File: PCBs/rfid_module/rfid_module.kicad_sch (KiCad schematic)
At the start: 0 parts

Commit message: RFID Module progress
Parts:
- added U101: Watch_Module_Outline_V1, watch_footprints:Watch Module Outline V1, symbol watch_symbols_lib:Watch_Module_Outline_V1
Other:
- added sheet Boost Converter (boost_converter.kicad_sch)
- added sheet Pogo Connector (pogo_connector.kicad_sch)
- added sheet STM32G0 (stm32g0.kicad_sch)
- sheet RFID ports: added CARRIER, OUT, OUTN, PULL, RF_IN, SHDN, VRF; removed none
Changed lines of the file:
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@@
 (kicad_sch (version 20230121) (generator eeschema)
   (paper "A4")
-  (sheet (at 121.92 66.04) (size 43.18 43.18) (fields_autoplaced)
-    (stroke (width 0.1524) (type solid))
-    (fill (color 0 0 0 0.0000))
-    (property "Sheetname" "RFID" (at 121.92 65.3284 0)
+  (wire (pts (xy 165.1 99.06) (xy 190.5 99.06))
+    (stroke (width 0) (type default))
+  )
+  (wire (pts (xy 165.1 101.6) (xy 190.5 101.6))
+    (stroke (width 0) (type default))
+  )
+  (wire (pts (xy 215.9 93.98) (xy 228.6 93.98))
+    (stroke (width 0) (type default))
+  )
+  (wire (pts (xy 104.14 78.74) (xy 129.54 78.74))
+    (stroke (width 0) (type default))
+  )
+  (wire (pts (xy 165.1 78.74) (xy 190.5 78.74))
+    (stroke (width 0) (type default))
+  )
+  (wire (pts (xy 228.6 78.74) (xy 228.6 93.98))
+    (stroke (width 0) (type default))
+  )
+  (wire (pts (xy 104.14 81.28) (xy 129.54 81.28))
+    (stroke (width 0) (type default))
+  )
+  (wire (pts (xy 165.1 104.14) (xy 190.5 104.14))
+    (stroke (width 0) (type default))
+  )
+  (wire (pts (xy 165.1 81.28) (xy 190.5 81.28))
+    (stroke (width 0) (type default))
+  )
+  (wire (pts (xy 215.9 78.74) (xy 228.6 78.74))
+    (stroke (width 0) (type default))
+  )
+  (wire (pts (xy 165.1 106.68) (xy 190.5 106.68))
+    (stroke (width 0) (type default))
+  )
+  (wire (pts (xy 165.1 96.52) (xy 190.5 96.52))
+    (stroke (width 0) (type default))
+  )
+  (wire (pts (xy 165.1 93.98) (xy 190.5 93.98))
+    (stroke (width 0) (type default))
+  )
+  (symbol (lib_id "watch_symbols_lib:Watch_Module_Outline_V1") (at 144.78 132.08 0) (unit 1)
+    (in_bom no) (on_board yes) (dnp no) (fields_autoplaced)
+    (property "Reference" "U101" (at 151.13 131.445 0)
+      (effects (font (size 1.27 1.27)) (justify left))
+    )
+    (property "Value" "Watch_Module_Outline_V1" (at 151.13 133.985 0)
+      (effects (font (size 1.27 1.27)) (justify left))
+    )
+    (property "Footprint" "watch_footprints:Watch Module Outline V1" (at 144.78 137.16 0)
+      (effects (font (size 1.27 1.27)) hide)
+    )
+    (property "Datasheet" "" (at 144.78 132.08 0)
+      (effects (font (size 1.27 1.27)) hide)
+    )
+    (instances
+      (project "rfid_module"
+        (path "/7f374643-2d66-4cfc-a525-255f058de0be"
+          (reference "U101") (unit 1)
+        )
+      )
+    )
+  )
+  (sheet (at 190.5 76.2) (size 25.4 7.62) (fields_autoplaced)
+    (stroke (width 0.1524) (type solid) (color 150 115 166 1))
+    (fill (color 225 213 231 1.0000))
+    (property "Sheetname" "Boost Converter" (at 190.5 75.4884 0)
       (effects (font (size 1.27 1.27)) (justify left bottom))
     )
-    (property "Sheetfile" "rfid.kicad_sch" (at 121.92 109.8046 0)
+    (property "Sheetfile" "boost_converter.kicad_sch" (at 190.5 84.4046 0)
       (effects (font (size 1.27 1.27)) (justify left top))
+    )
+    (pin "FB_OFFSET" input (at 190.5 78.74 180)
+      (effects (font (size 1.27 1.27)) (justify left))
+    )
+    (pin "VRF" output (at 215.9 78.74 0)
+      (effects (font (size 1.27 1.27)) (justify right))
+    )
+    (pin "EN" input (at 190.5 81.28 180)
+      (effects (font (size 1.27 1.27)) (justify left))
+    )
+    (instances
+      (project "rfid_module"
+        (path "/7f374643-2d66-4cfc-a525-255f058de0be" (page "5"))
+      )
+    )
+  )
+  (sheet (at 78.74 76.2) (size 25.4 30.48) (fields_autoplaced)
+    (stroke (width 0.1524) (type solid) (color 108 142 191 1))
+    (fill (color 218 232 252 1.0000))
+    (property "Sheetname" "Pogo Connector" (at 78.74 75.4884 0)
+      (effects (font (size 1.27 1.27)) (justify left bottom))
+    )
+    (property "Sheetfile" "pogo_connector.kicad_sch" (at 78.74 107.2646 0)
+      (effects (font (size 1.27 1.27)) (justify left top))
+    )
+    (pin "LPUART1_RX" input (at 104.14 81.28 0)
+      (effects (font (size 1.27 1.27)) (justify right))
+    )
+    (pin "LPUART1_TX" output (at 104.14 78.74 0)
+      (effects (font (size 1.27 1.27)) (justify right))
+    )
+    (instances
+      (project "rfid_module"
+        (path "/7f374643-2d66-4cfc-a525-255f058de0be" (page "4"))
+      )
+    )
+  )
+  (sheet (at 190.5 91.44) (size 25.4 17.78) (fields_autoplaced)
+    (stroke (width 0.1524) (type solid) (color 184 84 80 1))
+    (fill (color 248 206 204 1.0000))
+    (property "Sheetname" "RFID" (at 190.5 90.7284 0)
+      (effects (font (size 1.27 1.27)) (justify left bottom))
+    )
+    (property "Sheetfile" "rfid.kicad_sch" (at 190.5 109.8046 0)
+      (effects (font (size 1.27 1.27)) (justify left top))
+    )
+    (pin "SHDN" input (at 190.5 106.68 180)
+      (effects (font (size 1.27 1.27)) (justify left))
+    )
+    (pin "OUTN" input (at 190.5 96.52 180)
+      (effects (font (size 1.27 1.27)) (justify left))
+    )
+    (pin "OUT" input (at 190.5 93.98 180)
+      (effects (font (size 1.27 1.27)) (justify left))
+    )
+    (pin "RF_IN" output (at 190.5 99.06 180)
+      (effects (font (size 1.27 1.27)) (justify left))
+    )
+    (pin "CARRIER" output (at 190.5 101.6 180)
+      (effects (font (size 1.27 1.27)) (justify left))
+    )
+    (pin "PULL" input (at 190.5 104.14 180)
+      (effects (font (size 1.27 1.27)) (justify left))
+    )
+    (pin "VRF" input (at 215.9 93.98 0)
+      (effects (font (size 1.27 1.27)) (justify right))
     )
     (instances
@@
       )
     )
+  )
+  (sheet (at 129.54 76.2) (size 35.56 33.02) (fields_autoplaced)
+    (stroke (width 0.1524) (type solid) (color 130 179 102 1))
+    (fill (color 213 232 212 1.0000))
+    (property "Sheetname" "STM32G0" (at 129.54 75.4884 0)
+      (effects (font (size 1.27 1.27)) (justify left bottom))
+    )
+    (property "Sheetfile" "stm32g0.kicad_sch" (at 129.54 109.8046 0)
+      (effects (font (size 1.27 1.27)) (justify left top))
+    )
+    (pin "PULL" output (at 165.1 104.14 0)
+      (effects (font (size 1.27 1.27)) (justify right))
+    )
+    (pin "SWDIO" bidirectional (at 129.54 99.06 180)
+      (effects (font (size 1.27 1.27)) (justify left))
+    )
+    (pin "SHDN" output (at 165.1 106.68 0)
+      (effects (font (size 1.27 1.27)) (justify right))
+    )
+    (pin "SWCLK" input (at 129.54 96.52 180)
+      (effects (font (size 1.27 1.27)) (justify left))
+    )
+    (pin "TIM2_CH1" input (at 165.1 99.06 0)
+      (effects (font (size 1.27 1.27)) (justify right))
+    )
+    (pin "LPUART1_TX" output (at 129.54 78.74 180)
+      (effects (font (size 1.27 1.27)) (justify left))
+    )
+    (pin "LPUART1_RX" input (at 129.54 81.28 180)
+      (effects (font (size 1.27 1.27)) (justify left))
+    )
+    (pin "DAC1_OUT2" output (at 165.1 78.74 0)
+      (effects (font (size 1.27 1.27)) (justify right))
+    )
+    (pin "TIM1_CH1" output (at 165.1 93.98 0)
+      (effects (font (size 1.27 1.27)) (justify right))
+    )
+    (pin "TIM1_CH1N" output (at 165.1 96.52 0)
+      (effects (font (size 1.27 1.27)) (justify right))
+    )
+    (pin "NRST" output (at 129.54 101.6 180)
+      (effects (font (size 1.27 1.27)) (justify left))
+    )
+    (pin "BOOST_EN" output (at 165.1 81.28 0)
+      (effects (font (size 1.27 1.27)) (justify right))
+    )
+    (pin "COMP2_INP" input (at 165.1 101.6 0)
+      (effects (font (size 1.27 1.27)) (justify right))
+    )
+    (instances
+      (project "rfid_module"
+        (path "/7f374643-2d66-4cfc-a525-255f058de0be" (page "3"))
+      )
+    )

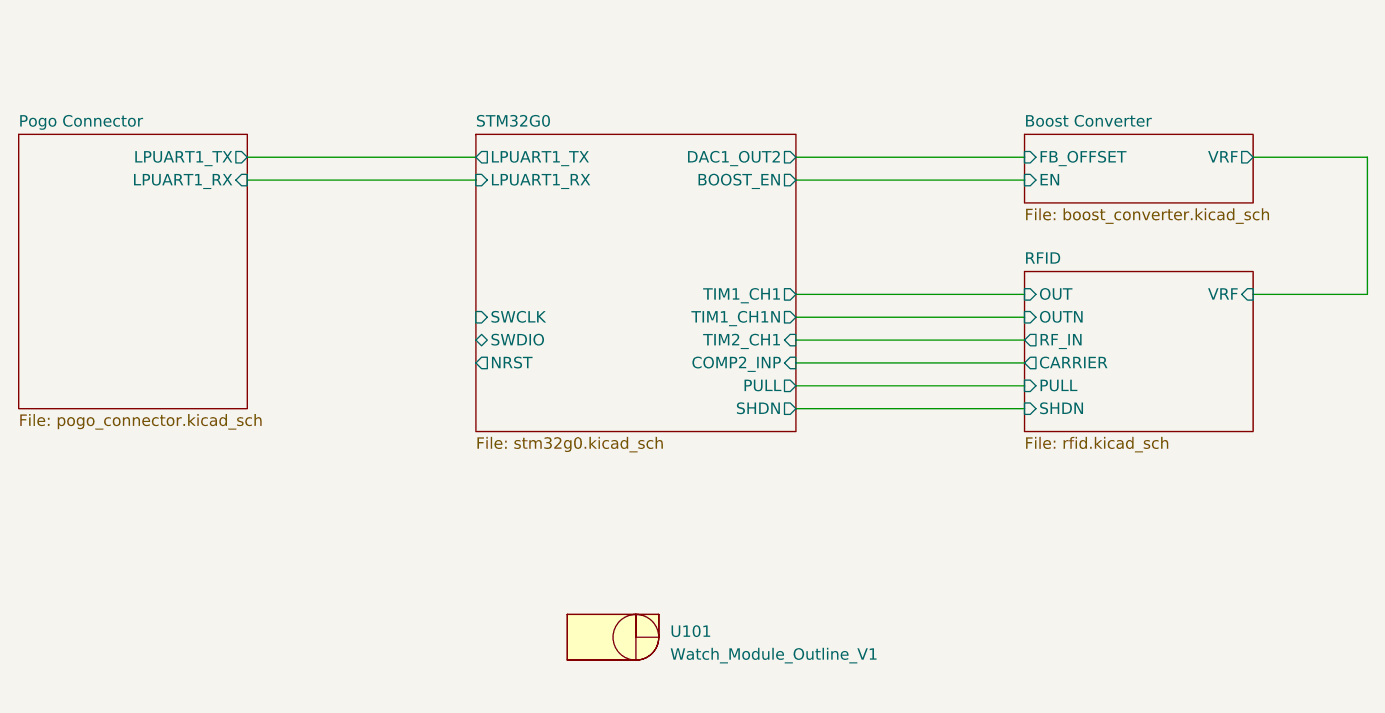
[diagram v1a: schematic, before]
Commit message: RFID PCB Done, started lower flex PCB
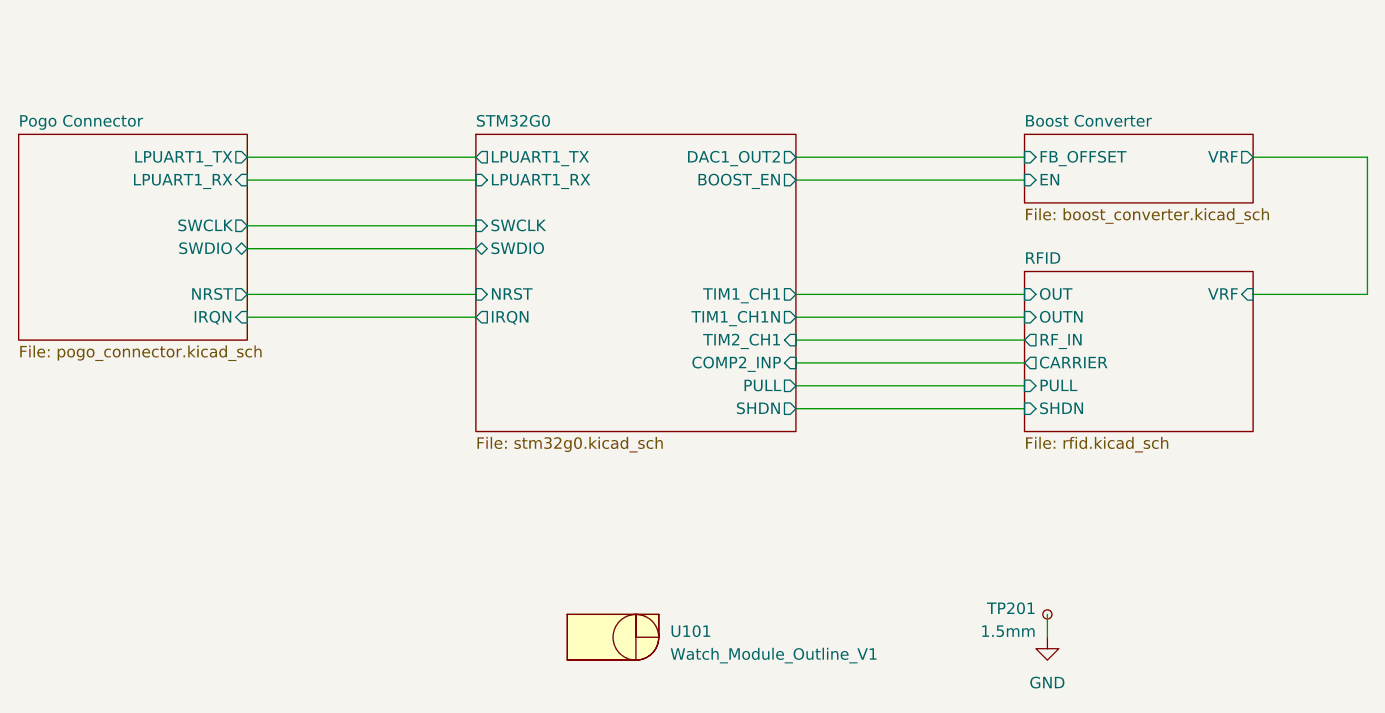
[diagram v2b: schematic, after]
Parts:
- added TP201: 1.5mm, TestPoint:TestPoint_Pad_D1.5mm, symbol Connector:TestPoint_Small
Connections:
- new net GND: TP201.1
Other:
- sheet Pogo Connector ports: added IRQN, NRST, SWCLK, SWDIO; removed none
- sheet STM32G0 ports: added IRQN; removed none
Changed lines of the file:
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@@
 (kicad_sch (version 20230121) (generator eeschema)
   (paper "A4")
+  (title_block
+    (date "2024-01-02")
+    (rev "1")
+  )
   (wire (pts (xy 165.1 99.06) (xy 190.5 99.06))
     (stroke (width 0) (type default))
@@
     (stroke (width 0) (type default))
   )
+  (wire (pts (xy 104.14 96.52) (xy 129.54 96.52))
+    (stroke (width 0) (type default))
+  )
+  (wire (pts (xy 104.14 93.98) (xy 129.54 93.98))
+    (stroke (width 0) (type default))
+  )
+  (wire (pts (xy 104.14 88.9) (xy 129.54 88.9))
+    (stroke (width 0) (type default))
+  )
+  (wire (pts (xy 104.14 86.36) (xy 129.54 86.36))
+    (stroke (width 0) (type default))
+  )
+  (wire (pts (xy 193.04 129.54) (xy 193.04 132.08))
+    (stroke (width 0) (type default))
+  )
   (wire (pts (xy 104.14 81.28) (xy 129.54 81.28))
     (stroke (width 0) (type default))
@@
   (wire (pts (xy 165.1 93.98) (xy 190.5 93.98))
     (stroke (width 0) (type default))
+  )
+  (symbol (lib_id "Connector:TestPoint_Small") (at 193.04 129.54 0) (mirror y) (unit 1)
+    (in_bom yes) (on_board yes) (dnp no)
+    (property "Reference" "TP201" (at 191.77 128.905 0)
+      (effects (font (size 1.27 1.27)) (justify left))
+    )
+    (property "Value" "1.5mm" (at 191.77 131.445 0)
+      (effects (font (size 1.27 1.27)) (justify left))
+    )
+    (property "Footprint" "TestPoint:TestPoint_Pad_D1.5mm" (at 187.96 129.54 0)
+      (effects (font (size 1.27 1.27)) hide)
+    )
+    (property "Datasheet" "~" (at 187.96 129.54 0)
+      (effects (font (size 1.27 1.27)) hide)
+    )
+    (pin "1")
+    (instances
+      (project "rfid_module"
+        (path "/7f374643-2d66-4cfc-a525-255f058de0be/a9cdb386-76ee-47d2-86a0-cb7dea8af18d"
+          (reference "TP201") (unit 1)
+        )
+        (path "/7f374643-2d66-4cfc-a525-255f058de0be"
+          (reference "TP101") (unit 1)
+        )
+      )
+      (project "watch_main"
+        (path "/b008648a-c7cf-4e14-8a0a-b9314d757b4a/8f147234-e39a-4c7c-8011-0af923cea553"
+          (reference "TP804") (unit 1)
+        )
+        (path "/b008648a-c7cf-4e14-8a0a-b9314d757b4a/e805c593-17ac-4f08-b6e2-d497b0af0a05"
+          (reference "TP1702") (unit 1)
+        )
+      )
+    )
   )
   (symbol (lib_id "watch_symbols_lib:Watch_Module_Outline_V1") (at 144.78 132.08 0) (unit 1)
@@
         (path "/7f374643-2d66-4cfc-a525-255f058de0be"
           (reference "U101") (unit 1)
+        )
+      )
+    )
+  )
+  (symbol (lib_id "power:GND") (at 193.04 132.08 0) (unit 1)
+    (in_bom yes) (on_board yes) (dnp no) (fields_autoplaced)
+    (property "Reference" "#PWR0210" (at 193.04 138.43 0)
+      (effects (font (size 1.27 1.27)) hide)
+    )
+    (property "Value" "GND" (at 193.04 137.16 0)
+      (effects (font (size 1.27 1.27)))
+    )
+    (property "Footprint" "" (at 193.04 132.08 0)
+      (effects (font (size 1.27 1.27)) hide)
+    )
+    (property "Datasheet" "" (at 193.04 132.08 0)
+      (effects (font (size 1.27 1.27)) hide)
+    )
+    (pin "1")
+    (instances
+      (project "rfid_module"
+        (path "/7f374643-2d66-4cfc-a525-255f058de0be/a9cdb386-76ee-47d2-86a0-cb7dea8af18d"
+          (reference "#PWR0210") (unit 1)
+        )
+        (path "/7f374643-2d66-4cfc-a525-255f058de0be"
+          (reference "#PWR0101") (unit 1)
+        )
+      )
+      (project "watch_main"
+        (path "/b008648a-c7cf-4e14-8a0a-b9314d757b4a/e805c593-17ac-4f08-b6e2-d497b0af0a05"
+          (reference "#PWR01710") (unit 1)
         )
       )
@@
     )
   )
-  (sheet (at 78.74 76.2) (size 25.4 30.48) (fields_autoplaced)
+  (sheet (at 78.74 76.2) (size 25.4 22.86) (fields_autoplaced)
     (stroke (width 0.1524) (type solid) (color 108 142 191 1))
     (fill (color 218 232 252 1.0000))
@@
       (effects (font (size 1.27 1.27)) (justify left bottom))
     )
-    (property "Sheetfile" "pogo_connector.kicad_sch" (at 78.74 107.2646 0)
+    (property "Sheetfile" "pogo_connector.kicad_sch" (at 78.74 99.6446 0)
       (effects (font (size 1.27 1.27)) (justify left top))
     )
@@
     )
     (pin "LPUART1_TX" output (at 104.14 78.74 0)
+      (effects (font (size 1.27 1.27)) (justify right))
+    )
+    (pin "SWCLK" output (at 104.14 86.36 0)
+      (effects (font (size 1.27 1.27)) (justify right))
+    )
+    (pin "SWDIO" bidirectional (at 104.14 88.9 0)
+      (effects (font (size 1.27 1.27)) (justify right))
+    )
+    (pin "IRQN" input (at 104.14 96.52 0)
+      (effects (font (size 1.27 1.27)) (justify right))
+    )
+    (pin "NRST" output (at 104.14 93.98 0)
       (effects (font (size 1.27 1.27)) (justify right))
     )
@@
       (effects (font (size 1.27 1.27)) (justify right))
     )
-    (pin "SWDIO" bidirectional (at 129.54 99.06 180)
+    (pin "SWDIO" bidirectional (at 129.54 88.9 180)
       (effects (font (size 1.27 1.27)) (justify left))
     )
@@
       (effects (font (size 1.27 1.27)) (justify right))
     )
-    (pin "SWCLK" input (at 129.54 96.52 180)
+    (pin "SWCLK" input (at 129.54 86.36 180)
       (effects (font (size 1.27 1.27)) (justify left))
     )
@@
       (effects (font (size 1.27 1.27)) (justify right))
     )
-    (pin "NRST" output (at 129.54 101.6 180)
-      (effects (font (size 1.27 1.27)) (justify left))
-    )
     (pin "BOOST_EN" output (at 165.1 81.28 0)
       (effects (font (size 1.27 1.27)) (justify right))
@@
       (effects (font (size 1.27 1.27)) (justify right))
     )
-    (instances
+    (pin "IRQN" output (at 129.54 96.52 180)
+      (effects (font (size 1.27 1.27)) (justify left))
+    )
+    (pin "NRST" input (at 129.54 93.98 180)
+      (effects (font (size 1.27 1.27)) (justify left))
+    )
+    (instances
